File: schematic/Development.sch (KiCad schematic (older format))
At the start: 94 parts

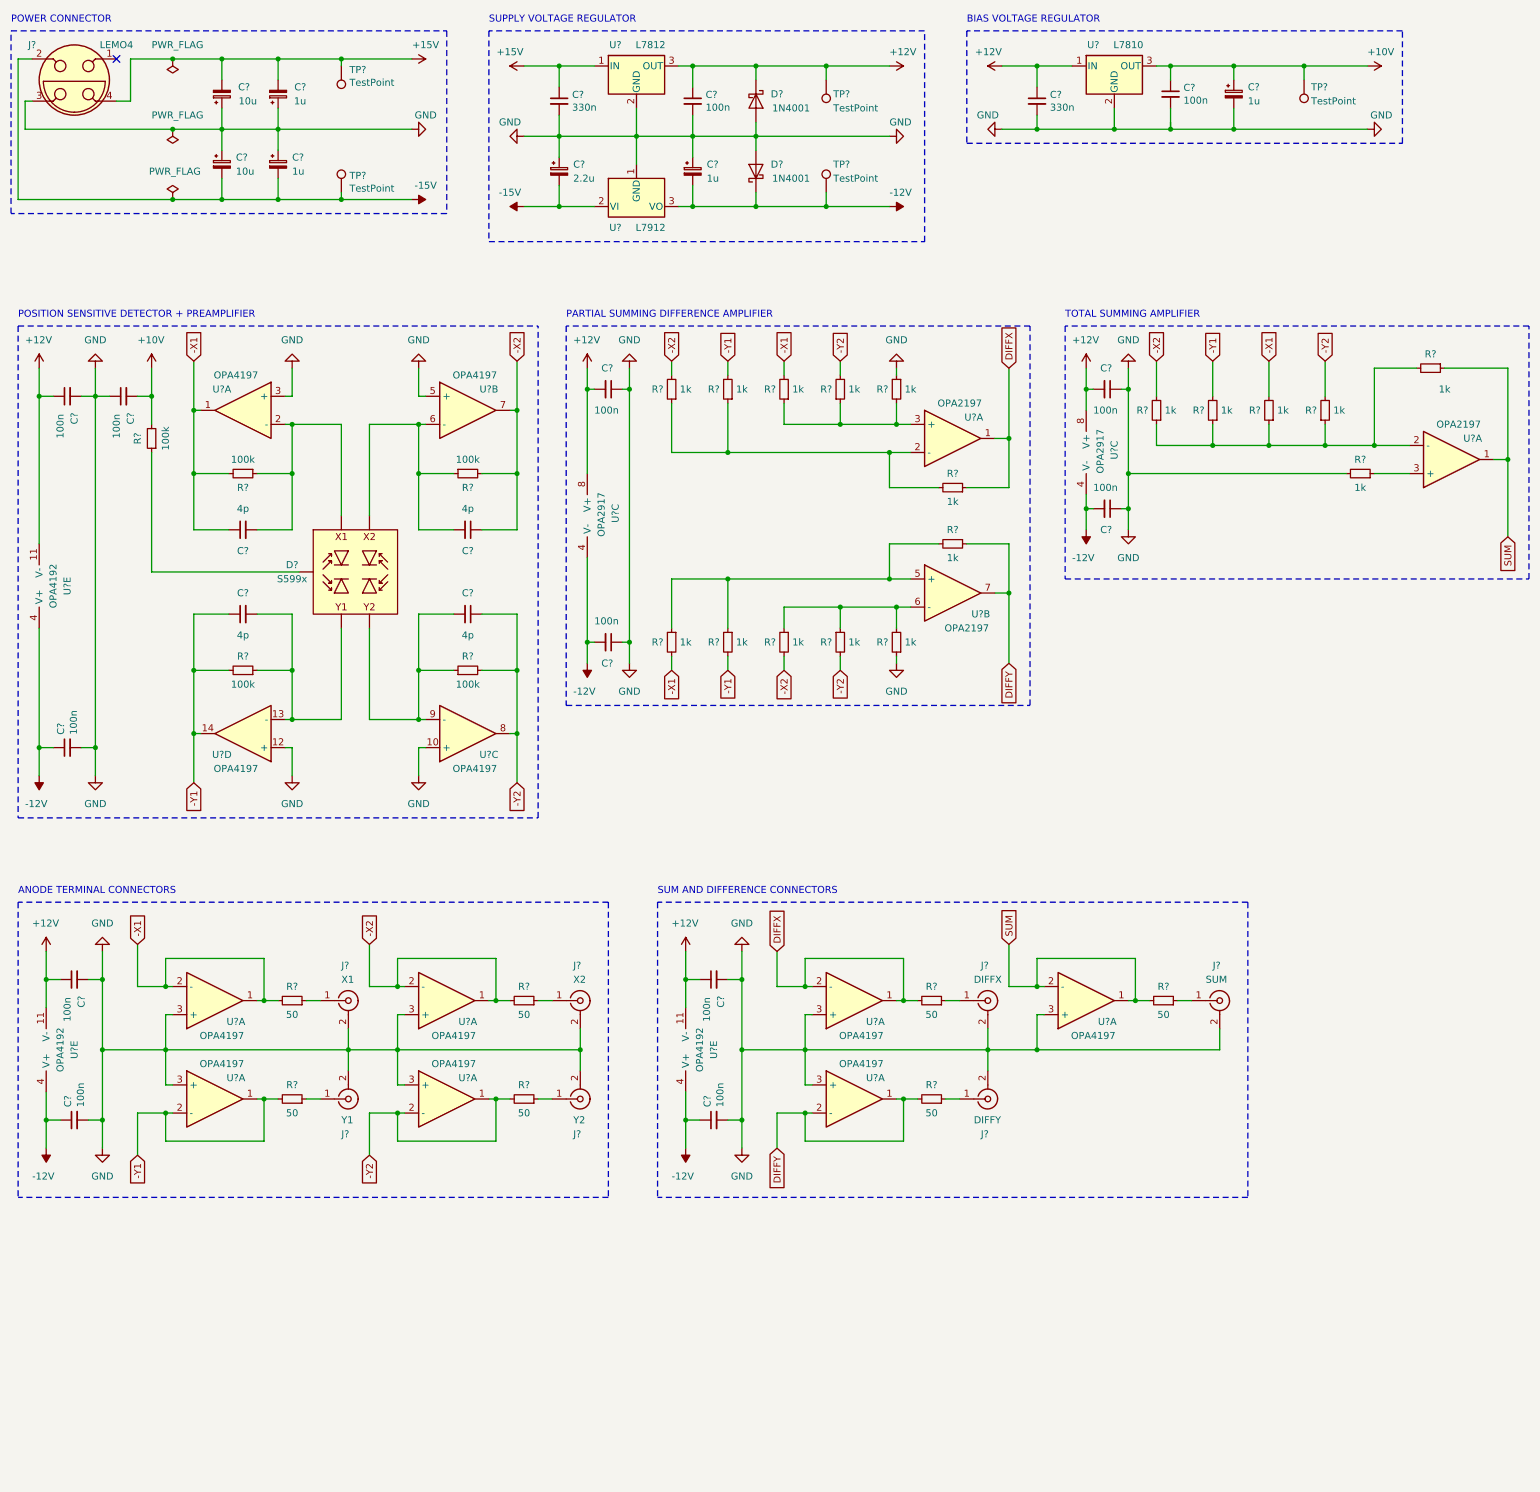
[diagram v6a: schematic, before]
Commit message: replaced lemo with 3pin connector, created linear arthimetic amplifier section
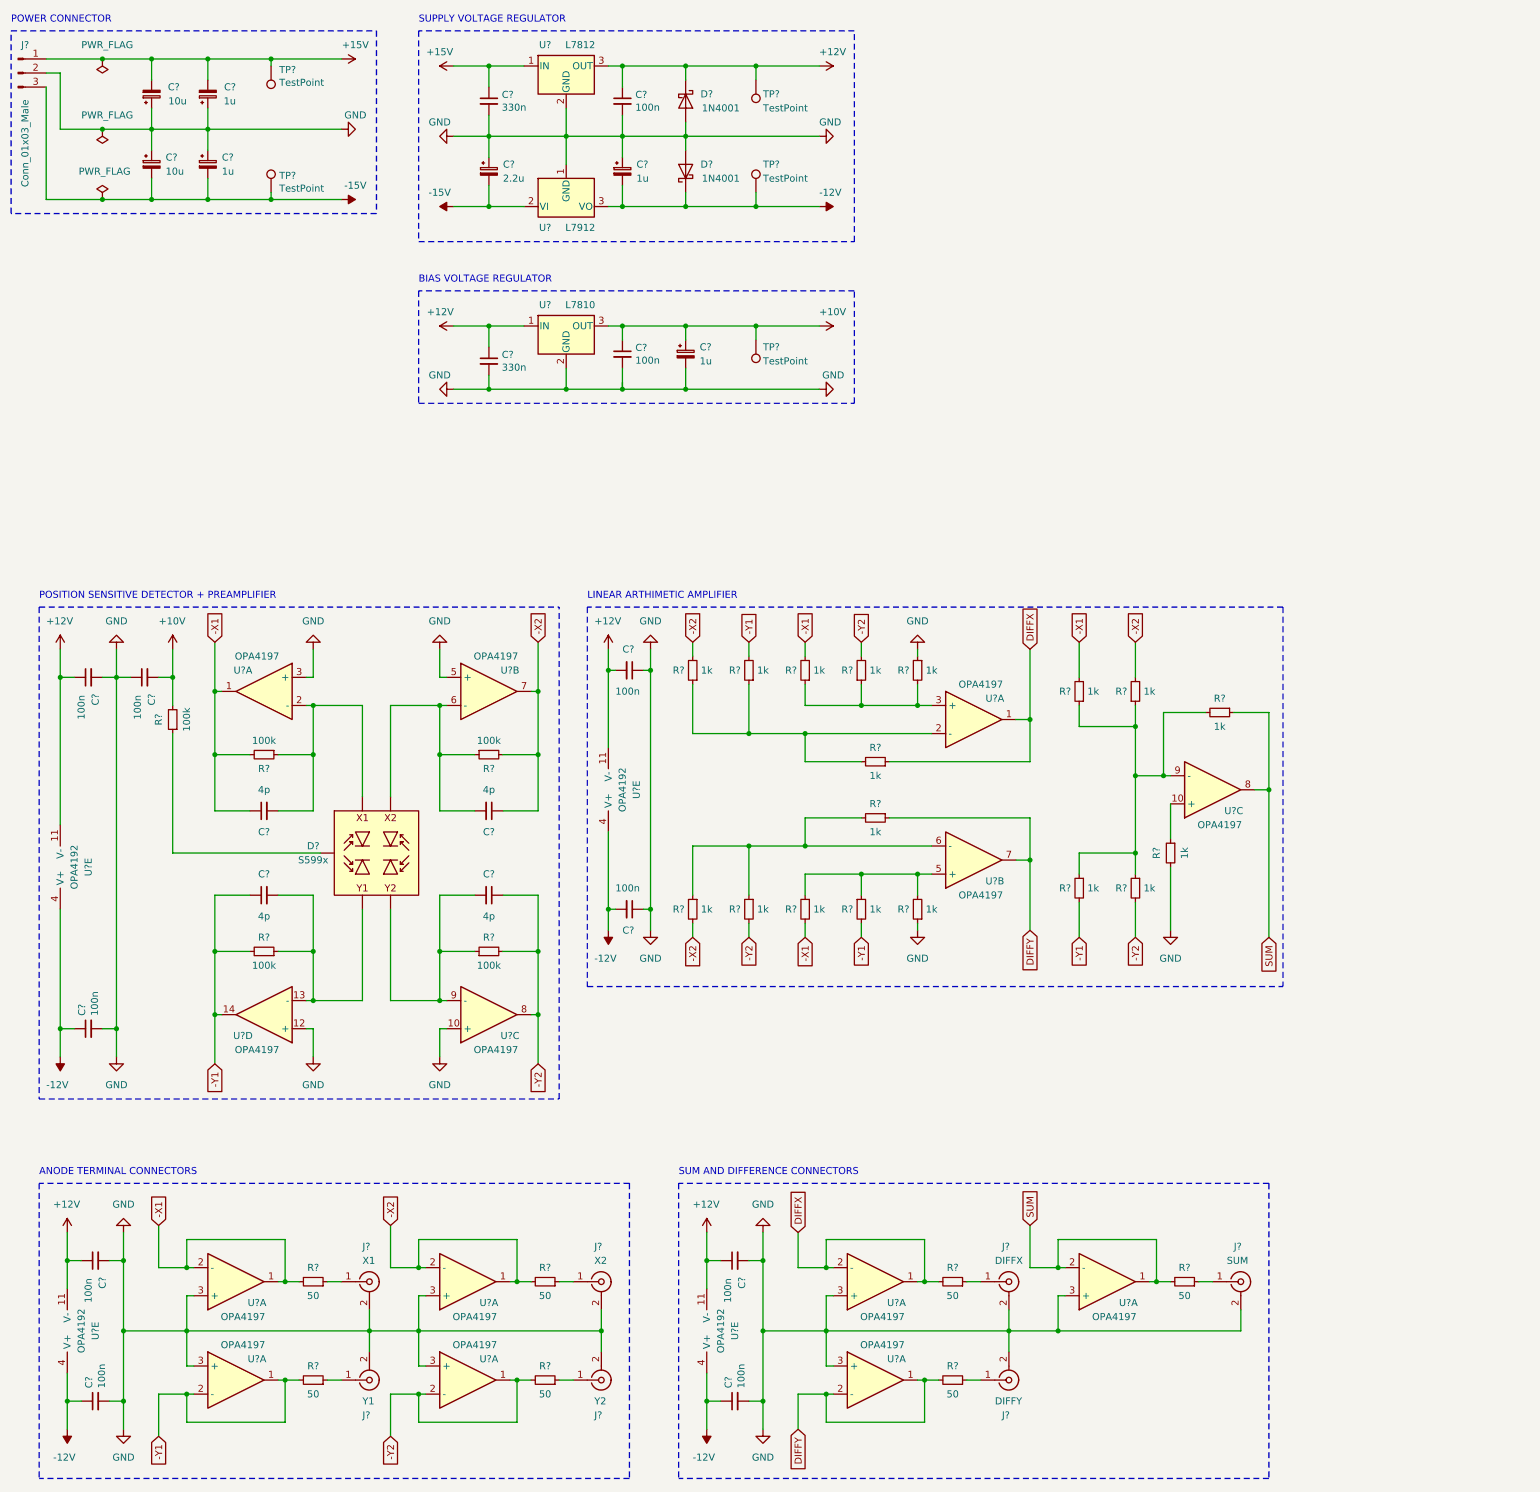
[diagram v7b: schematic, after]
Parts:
- removed C? (x2): 100n, symbol Development-rescue:C_Small-Device
- removed J?: LEMO4, symbol Development-rescue:LEMO4-Connector
- removed U? (x3): OPA2197, symbol Development-rescue:Opamp_Dual_Generic-Device
- removed U? (x2): OPA2917, symbol Development-rescue:Opamp_Dual_Generic-Device
- added J?: Conn_01x03_Male, symbol Connector:Conn_01x03_Male
- added U?: OPA4192, symbol Development-rescue:Opamp_Quad_Generic-Device
- added U? (x3): OPA4197, symbol Development-rescue:Opamp_Quad_Generic-Device
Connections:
- net +12V: now also U?.11 (V-)
- net +15V: now also J?.1 (Pin_1)
- net -12V: now also U?.4 (V+)
- net -15V: now also J?.3 (Pin_3)
- net -X1: now also R?.2; no longer R?.2
- net -X2: now also R?.2, R?.2; no longer R?.2, R?.2
- net -Y1: now also R?.2, R?.2; no longer R?.2, R?.2
- net -Y2: now also R?.2, R?.2; no longer R?.2, R?.2
- net DIFFX: now also U?.1
- net DIFFY: now also U?.7
- net GND: now also J?.2 (Pin_2)
- net SUM: now also U?.8
- net at R?.1, R?.1, R?.2: now also U?.2 (-)
- net at R?.1, R?.1, R?.2: now also U?.3 (+)
- net at R?.1, R?.1, R?.2: now also U?.6 (-)
- net at R?.1, R?.1, R?.2: now also U?.5 (+)
- net at R?.1, R?.1, R?.1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: now also U?.9 (-)
- net at R?.1: now also U?.10 (+)
- no-connect marks 1 -> 0
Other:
- note added: "LINEAR ARTHIMETIC AMPLIFIER"
- note removed: "PARTIAL SUMMING DIFFERENCE AMPLIFIER"
- note removed: "TOTAL SUMMING AMPLIFIER"
- moved on the sheet: C?, D?, J?, R?, TP?, U?, U?A, U?B, U?C, U?D, U?E

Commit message: added analog divider and connectors
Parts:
- added C? (x2): 100n, symbol Development-rescue:C_Small-Device
- added D? (x2): 1N4148, Diode_THT:D_DO-35_SOD27_P7.62mm_Horizontal, symbol Diode:1N4148
- added J?: X, symbol Connector:Conn_Coaxial
- added J?: Y, symbol Connector:Conn_Coaxial
- added R? (x2): 50, symbol Development-rescue:R_Small-Device
- added U? (x2): AD538, symbol Library:AD538
- added U? (x3): OPA2197, symbol Development-rescue:Opamp_Dual_Generic-Device
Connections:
- net +12V: now also C?.1, U?.8 (V+)
- net +15V: now also U?.6 (+Vs), U?.6 (+Vs)
- net -12V: now also C?.1, U?.4 (V-)
- net -15V: now also U?.7 (-Vs), U?.7 (-Vs)
- net DIFFX: now also U?.2 (Vz)
- net DIFFY: now also U?.2 (Vz)
- net GND: now also C?.2, C?.2, D?.1 (K), D?.1 (K), J?.2 (Ext), J?.2 (Ext), U?.13 (PWR_GND), U?.13 (PWR_GND), U?.14 (SIG_GND), U?.14 (SIG_GND), U?.3 (+), U?.6 (-)
- net SUM: now also U?.15 (Vx), U?.15 (Vx)
- new net: U?.10 (Vy), U?.4 (+10V) (x2)
- new net: D?.2 (A), U?.11 (Iy) (x2)
- new net: U?.12 (C), U?.3 (B) (x2)
- new net: J?.1 (In), R?.1 (x2)
- new net X: R?.2, U?.1, U?.2 (-), U?.8 (Vo)
- new net Y: R?.2, U?.5 (+), U?.7, U?.8 (Vo)
- no-connect marks 0 -> 12
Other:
- note added: "DIVISION ARTHIMETIC"
- note added: "LINEAR ARTHIMETIC"
- note added: "POSITION CONNECTORS"
- note added: "POSITION SENSITIVE DETECTOR AND TRANSIMPEDANCE MPLIFIER"
- note removed: "LINEAR ARTHIMETIC AMPLIFIER"
- note removed: "POSITION SENSITIVE DETECTOR + PREAMPLIFIER"
- moved on the sheet: C?, D?, J?, R?, TP?, U?, U?A, U?B, U?C, U?D, U?E
